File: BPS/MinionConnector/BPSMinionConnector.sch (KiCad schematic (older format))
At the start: 42 parts, among them J1 TempConn2, J10 TempConn9, J11 TempConn10, J12 TempConn11, J13 TempConn12, J14 TempConn2, J15 TempConn13, J16 TempConn14, J17 TempConn15, J18 TempConn16, J2 TempConn3, J3 TempConn4, J4 TempConn5, J5 TempConn6, J6 TempConn7, J7 TempConn1, J8 TempConn8, J9 TempConn2

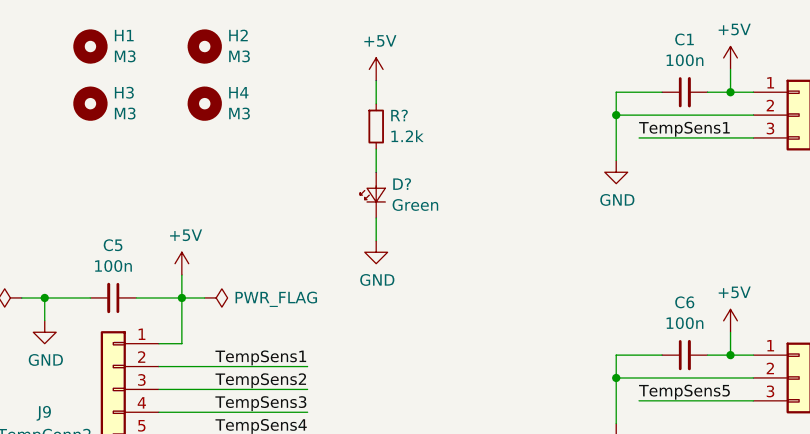
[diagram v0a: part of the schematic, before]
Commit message: Adds pdf schematics of Minion boards.
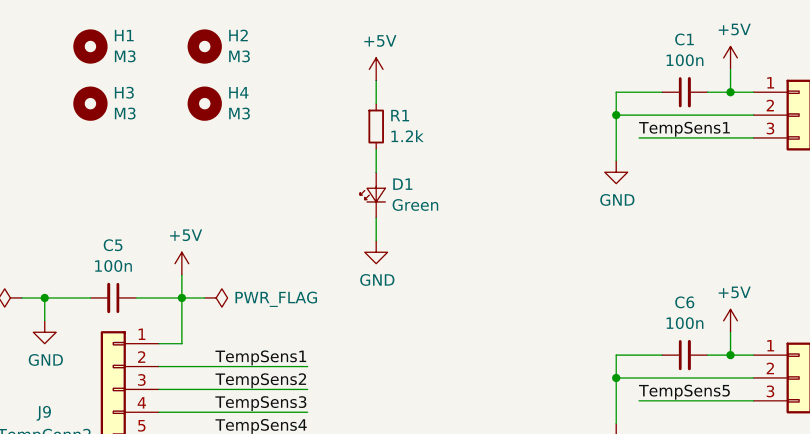
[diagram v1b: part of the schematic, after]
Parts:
- gave numbers to parts that had none: 2
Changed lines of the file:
@@
 $EndComp
 $Comp
-L Device:R_Small R?
+L Device:R_Small R1
 U 1 1 5DC78BA1
 P 2750 1350
-F 0 "R?" H 2809 1396 50  0000 L CNN
+F 0 "R1" H 2809 1396 50  0000 L CNN
 F 1 "1.2k" H 2809 1305 50  0000 L CNN
 F 2 "Resistor_SMD:R_0805_2012Metric" H 2750 1350 50  0001 C CNN
@@
 $EndComp
 $Comp
-L Device:LED_Small D?
+L Device:LED_Small D1
 U 1 1 5DC7A4AC
 P 2750 1650
-F 0 "D?" V 2796 1582 50  0000 R CNN
+F 0 "D1" V 2796 1582 50  0000 R CNN
 F 1 "Green" V 2705 1582 50  0000 R CNN
 F 2 "LED_SMD:LED_0805_2012Metric" V 2750 1650 50  0001 C CNN
@@
 	2750 1550 2750 1450
 $Comp
-L power:GND #PWR?
+L power:GND #PWR0139
 U 1 1 5DC82274
 P 2750 1850
-AR Path="/5DC82274" Ref="#PWR?"  Part="1"
+AR Path="/5DC82274" Ref="#PWR0139"  Part="1"
 AR Path="/5DF406D3/5DC82274" Ref="#PWR?"  Part="1"
-F 0 "#PWR?" H 2750 1600 50  0001 C CNN
+F 0 "#PWR0139" H 2750 1600 50  0001 C CNN
 F 1 "GND" H 2755 1677 50  0000 C CNN
 F 2 "" H 2750 1850 50  0001 C CNN
@@
 	2750 1850 2750 1750
 $Comp
-L power:+5V #PWR?
+L power:+5V #PWR0140
 U 1 1 5DC8996B
 P 2750 1150
-AR Path="/5DC8996B" Ref="#PWR?"  Part="1"
+AR Path="/5DC8996B" Ref="#PWR0140"  Part="1"
 AR Path="/5DF406D3/5DC8996B" Ref="#PWR?"  Part="1"
-F 0 "#PWR?" H 2750 1000 50  0001 C CNN
+F 0 "#PWR0140" H 2750 1000 50  0001 C CNN
 F 1 "+5V" H 2765 1323 50  0000 C CNN
 F 2 "" H 2750 1150 50  0001 C CNN
